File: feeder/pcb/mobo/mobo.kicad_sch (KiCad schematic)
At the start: 60 parts, among them J1 SWD_10, J2 FTDI_HEADER, J3 PLATED_PADS, M1 PEEL_MOTOR, M2 DRIVE_MOTOR, SW1 RESET, SW2 BUTTON_1, SW3 BUTTON_2, SW4 BOOT, U1 QRE1113GR, U2 STM32F103C8Tx, U3 TCS40DPR, U4 AP1117-33, U5 MCP16301, U6 DRV8833PWP, U7 MAX3078E, Y1 8MHz

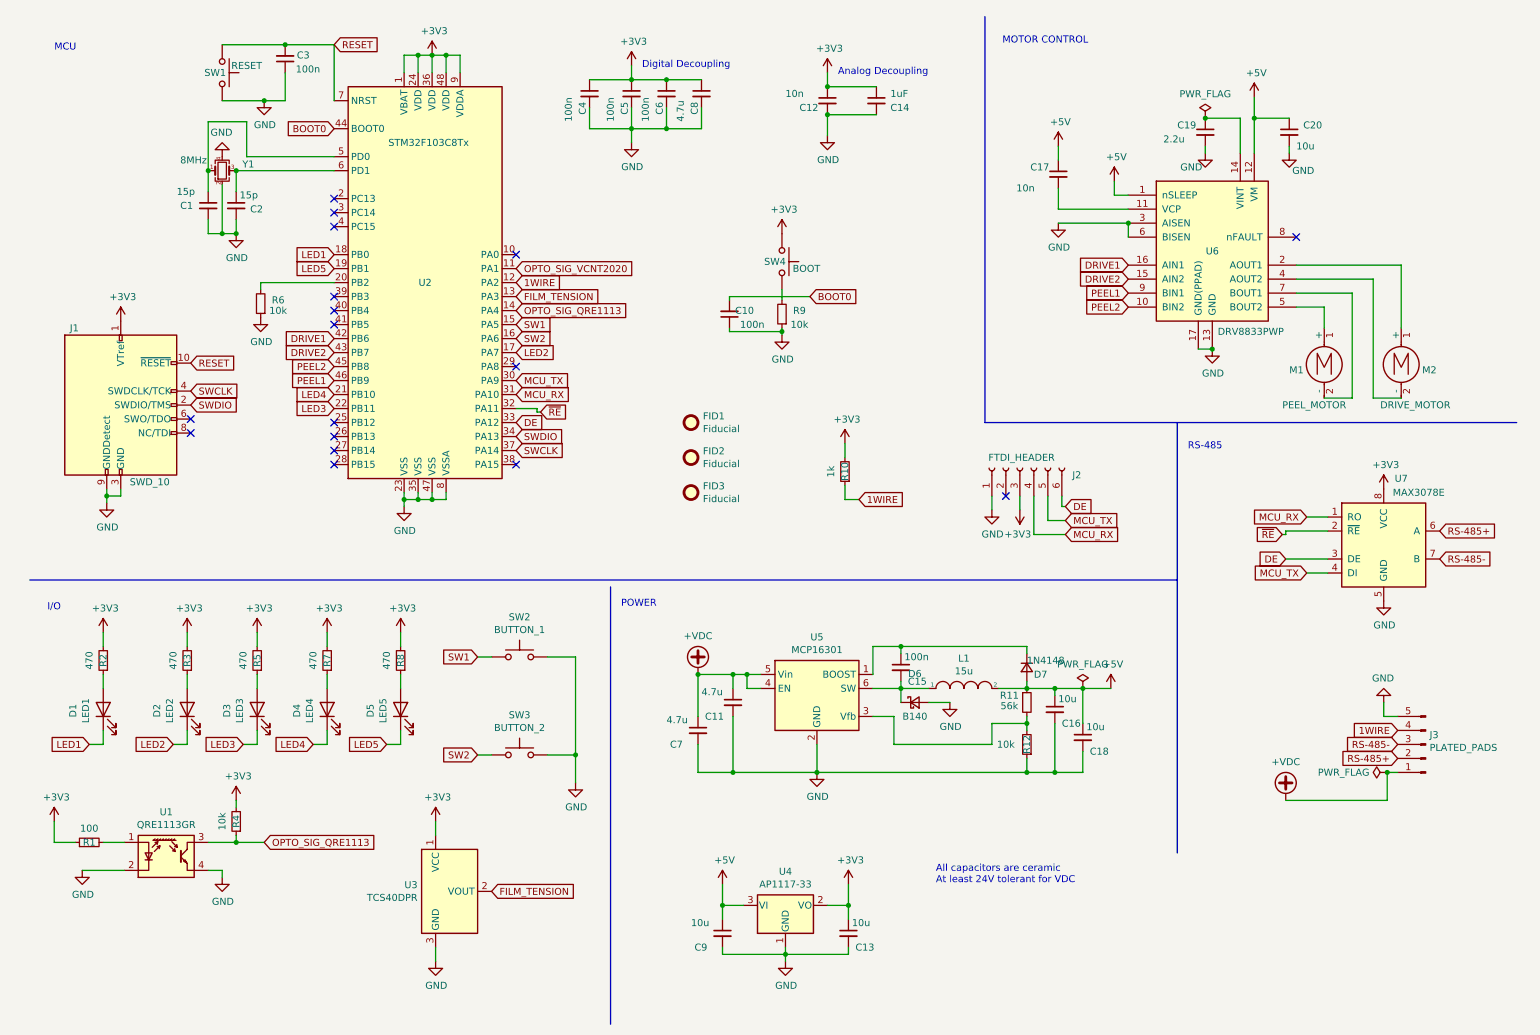
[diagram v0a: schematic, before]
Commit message: reworked feeder pcb to have minimal dimensions, more available parts, and swappable uC options
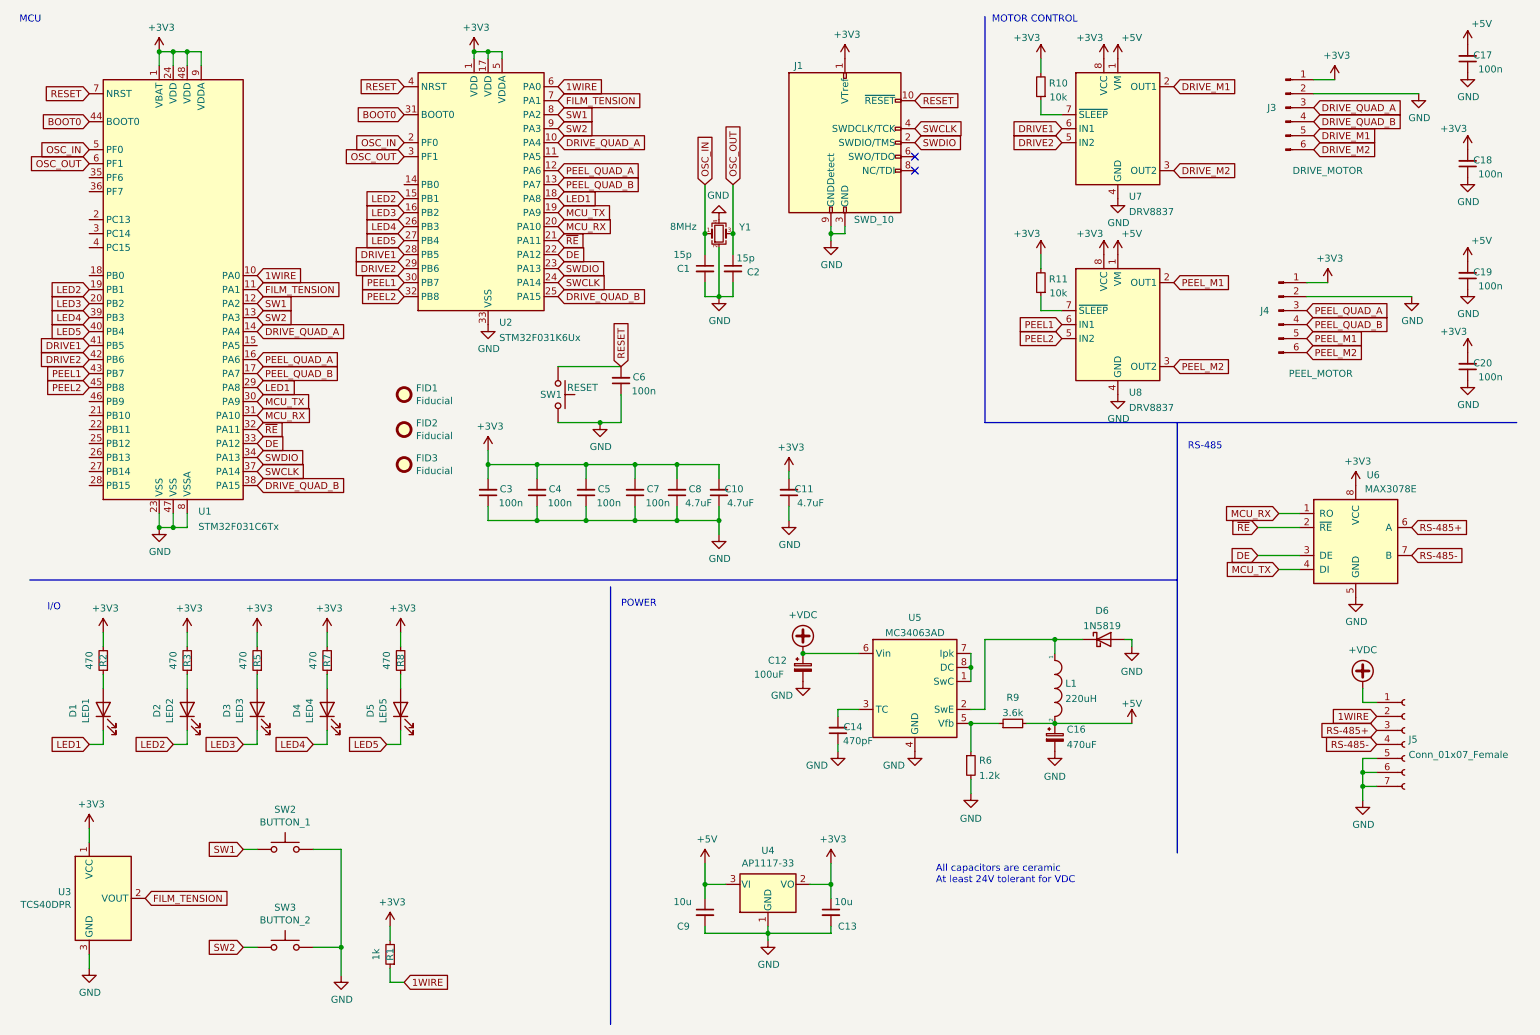
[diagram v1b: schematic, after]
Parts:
- removed C12: 10n, Capacitor_SMD:C_0805_2012Metric, symbol Device:C_Small
- removed C15: 100n, Capacitor_SMD:C_0805_2012Metric, symbol Device:C_Small
- removed C16: 10u, Capacitor_SMD:C_0805_2012Metric, symbol Device:C_Small
- removed D6: B140, Diode_SMD:D_SMB_Handsoldering, symbol Device:D_Schottky_Small
- removed D7: 1N4148, Diode_SMD:D_SOD-123, symbol Device:D_Small
- removed J2: FTDI_HEADER, Connector_PinHeader_2.54mm:PinHeader_1x06_P2.54mm_Vertical, symbol Connector:Conn_01x06_Female
- removed J3: PLATED_PADS, index:5-pad-spring-finger-interface, symbol Connector:Conn_01x05_Male
- removed M1: PEEL_MOTOR, Connector_PinHeader_2.54mm:PinHeader_1x02_P2.54mm_Vertical, symbol Motor:Motor_DC
- removed M2: DRIVE_MOTOR, Connector_PinHeader_2.54mm:PinHeader_1x02_P2.54mm_Vertical, symbol Motor:Motor_DC
- removed R12, R4: 10k, Resistor_SMD:R_0805_2012Metric, symbol Device:R_Small
- removed SW4: BOOT, Button_Switch_SMD:Panasonic_EVQPUJ_EVQPUA, symbol Switch:SW_Push
- removed U1: QRE1113GR, OptoDevice:OnSemi_CASE100CY, symbol Sensor_Proximity:QRE1113GR
- removed U2: STM32F103C8Tx, Package_QFP:LQFP-48_7x7mm_P0.5mm, symbol MCU_ST_STM32F1:STM32F103C8Tx
- removed U5: MCP16301, Package_TO_SOT_SMD:SOT-23-6, symbol Regulator_Switching:MCP16301
- removed U6: DRV8833PWP, Package_SO:HTSSOP-16-1EP_4.4x5mm_P0.65mm_EP3.4x5mm_Mask2.46x2.31mm_ThermalVias, symbol Driver_Motor:DRV8833PWP
- removed U7: MAX3078E, Package_SO:SOIC-8_3.9x4.9mm_P1.27mm, symbol Interface_UART:MAX3078E
- added C12: 100uF, Capacitor_SMD:C_Elec_5x5.8, symbol Device:C_Polarized_Small
- added C16: 470uF, Capacitor_SMD:C_Elec_5x5.8, symbol Device:C_Polarized_Small
- added D6: 1N5819, Diode_SMD:D_SOD-123, symbol Diode:1N5819
- added J3: DRIVE_MOTOR, Connector_PinHeader_2.54mm:PinHeader_1x06_P2.54mm_Vertical, symbol Connector:Conn_01x06_Male
- added J4: PEEL_MOTOR, Connector_PinHeader_2.54mm:PinHeader_1x06_P2.54mm_Vertical, symbol Connector:Conn_01x06_Male
- added J5: Conn_01x07_Female, index:AVX-9155-005-541, symbol Connector:Conn_01x07_Female
- added U1: STM32F031C6Tx, Package_QFP:LQFP-48_7x7mm_P0.5mm, symbol MCU_ST_STM32F0:STM32F031C6Tx
- added U2: STM32F031K6Ux, Package_DFN_QFN:QFN-32-1EP_5x5mm_P0.5mm_EP3.45x3.45mm, symbol MCU_ST_STM32F0:STM32F031K6Ux
- added U5: MC34063AD, Package_SO:SOIC-8_3.9x4.9mm_P1.27mm, symbol Regulator_Switching:MC34063AD
- added U6: MAX3078E, Package_SO:SOIC-8_3.9x4.9mm_P1.27mm, symbol Interface_UART:MAX3078E
- added U7, U8: DRV8837, Package_SON:WSON-8-1EP_2x2mm_P0.5mm_EP0.9x1.6mm, symbol Driver_Motor:DRV8837
- C10: value 100n -> 4.7uF
- C11, C8: value 4.7u -> 4.7uF; JLCPCB C1779 -> C49678; LCSC C98192 -> C476766
- C14: value 1uF -> 470pF; JLCPCB C28323 -> C49678; LCSC C16834 -> C476766
- C17: value 10n -> 100n; JLCPCB C1710 -> C49678; LCSC C83170 -> C476766
- C18, C20: value 10u -> 100n; JLCPCB C15850 -> C49678; LCSC C17024 -> C476766
- C19: value 2.2u -> 100n; JLCPCB C49217 -> C49678; LCSC C84716 -> C476766
- C7: value 4.7u -> 100n; JLCPCB C1779 -> C49678; LCSC C98192 -> C476766
- L1: value 15u -> 220uH; footprint Inductor_SMD:L_Taiyo-Yuden_NR-50xx_HandSoldering -> Inductor_SMD:L_6.3x6.3_H3; JLCPCB C44888 -> (none); LCSC C44888 -> (none)
- R1: value 100 -> 1k; JLCPCB C17408 -> C17513; LCSC C25277 -> C17513
- R10: value 1k -> 10k; JLCPCB C17513 -> C17414; LCSC C17513 -> C25612
- R11: value 56k -> 10k; JLCPCB C25638 -> C17414; LCSC C25638 -> C25612
- R6: value 10k -> 1.2k; JLCPCB C17414 -> (none); LCSC C25612 -> (none)
- R9: value 10k -> 3.6k; JLCPCB C17414 -> (none); LCSC C25612 -> (none)
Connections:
- net +3V3: now also C10.2, C11.2, C18.2, C20.2, C3.2, C4.2, C5.2, C7.2, C8.2, R1.2, R11.2, J3.1 (Pin_1), J4.1 (Pin_1), U1.1 (VBAT), U1.24 (VDD), U1.48 (VDD), U1.9 (VDDA), U2.1 (VDD), U2.17 (VDD), U2.5 (VDDA), U6.8 (VCC), U7.8 (VCC), U8.8 (VCC); no longer C14.1, C4.1, C5.1, C6.1, C8.1, R1.1
- net +5V: now also C17.2, C19.2, R9.2, C16.1, U7.1 (VM), U8.1 (VM); no longer C17.1, C18.1, C20.1, R11.1
- net +VDC: now also C12.1, J5.1 (Pin_1), U5.6 (Vin); no longer C11.1, C7.1
- net 1WIRE: now also R1.1, J5.2 (Pin_2), U1.10 (PA0), U2.6 (PA0); no longer R10.1
- net BOOT0: now also U1.44 (BOOT0), U2.31 (BOOT0); no longer C10.2
- net DE: now also U1.33 (PA12), U2.22 (PA12), U6.3 (DE)
- net DRIVE1: now also U1.41 (PB5), U2.28 (PB5), U7.6 (IN1)
- net DRIVE2: now also U1.42 (PB6), U2.29 (PB6), U7.5 (IN2)
- net FILM_TENSION: now also U1.11 (PA1), U2.7 (PA1)
- net GND: now also C11.1, C14.1, C17.1, C18.1, C19.1, C20.1, C4.1, C5.1, C6.1, C7.1, C8.1, R6.2, C12.2, C16.2, D6.2 (A), J3.2 (Pin_2), J4.2 (Pin_2), J5.5 (Pin_5), J5.6 (Pin_6), J5.7 (Pin_7), U1.23 (VSS), U1.47 (VSS), U1.8 (VSSA), U2.33 (VSS), U5.4 (GND), U6.5 (GND), U7.4 (GND), U7.9 (GND), U8.4 (GND), U8.9 (GND); no longer C11.2, C14.2, C18.2, C19.2, C20.2, C4.2, C5.2, C6.2, C7.2, C8.2, R6.1, R9.1
- net LED1: now also U1.29 (PA8), U2.18 (PA8)
- net LED2: now also U1.19 (PB1), U2.15 (PB1)
- net LED3: now also U1.20 (PB2), U2.16 (PB2)
- net LED4: now also U1.39 (PB3), U2.26 (PB3)
- net LED5: now also U1.40 (PB4), U2.27 (PB4)
- net MCU_RX: now also U1.31 (PA10), U2.20 (PA10), U6.1 (RO)
- net MCU_TX: now also U1.30 (PA9), U2.19 (PA9), U6.4 (DI)
- net PEEL1: now also U1.43 (PB7), U2.30 (PB7), U8.6 (IN1)
- net PEEL2: now also U1.45 (PB8), U2.32 (PB8), U8.5 (IN2)
- net RESET: now also C6.2, U1.7 (NRST), U2.4 (NRST); no longer C3.2
- net RS-485+: now also J5.3 (Pin_3), U6.6 (A)
- net RS-485-: now also J5.4 (Pin_4), U6.7 (B)
- net SW1: now also U1.12 (PA2), U2.8 (PA2)
- net SW2: now also U1.13 (PA3), U2.9 (PA3)
- net SWCLK: now also U1.37 (PA14), U2.24 (PA14)
- net SWDIO: now also U1.34 (PA13), U2.23 (PA13)
- net ~{RE}: now also U1.32 (PA11), U2.21 (PA11), U6.2 (~{RE})
- net OSC_IN: now reaches C1.1, Y1.1
- net OSC_IN: now also U1.5 (PF0), U2.2 (PF0)
- net OSC_OUT: now reaches C2.1, Y1.3
- net OSC_OUT: now also U1.6 (PF1), U2.3 (PF1)
- net at L1.1: now also D6.1 (K), U5.2 (SwE)
- new net: R11.1, U8.7 (~{SLEEP})
- new net: R10.1, U7.7 (~{SLEEP})
- new net: R6.1, R9.1, U5.5 (Vfb)
- new net: C14.2, U5.3 (TC)
- new net: U5.1 (SwC), U5.7 (Ipk), U5.8 (DC)
- new net DRIVE_M1: J3.5 (Pin_5), U7.2 (OUT1)
- new net DRIVE_M2: J3.6 (Pin_6), U7.3 (OUT2)
- new net DRIVE_QUAD_A: J3.3 (Pin_3), U1.14 (PA4), U2.10 (PA4)
- new net DRIVE_QUAD_B: J3.4 (Pin_4), U1.38 (PA15), U2.25 (PA15)
- new net PEEL_M1: J4.5 (Pin_5), U8.2 (OUT1)
- new net PEEL_M2: J4.6 (Pin_6), U8.3 (OUT2)
- new net PEEL_QUAD_A: J4.3 (Pin_3), U1.16 (PA6), U2.12 (PA6)
- new net PEEL_QUAD_B: J4.4 (Pin_4), U1.17 (PA7), U2.13 (PA7)
- no-connect marks 17 -> 2
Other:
- note removed: "Analog Decoupling"
- note removed: "Digital Decoupling"
- moved on the sheet: C1, C2, FID1, FID2, FID3, J1, SW2, SW3, U3, Y1
